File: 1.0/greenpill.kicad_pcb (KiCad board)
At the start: 4 copper layers, 17.4 x 53.1 mm, 33 parts, among them J1 Conn_01x20_Male, J2 Conn_01x20_Male, J3 Conn_01x04_Male, J5 USB_C_Receptacle_USB2.0, SW1 SW_Push, SW2 SW_Push, U1 ATSAMD51J20A-M, U2 MIC5504-3.3YM5, U3 S25FL064, Y1 Crystal_GND23

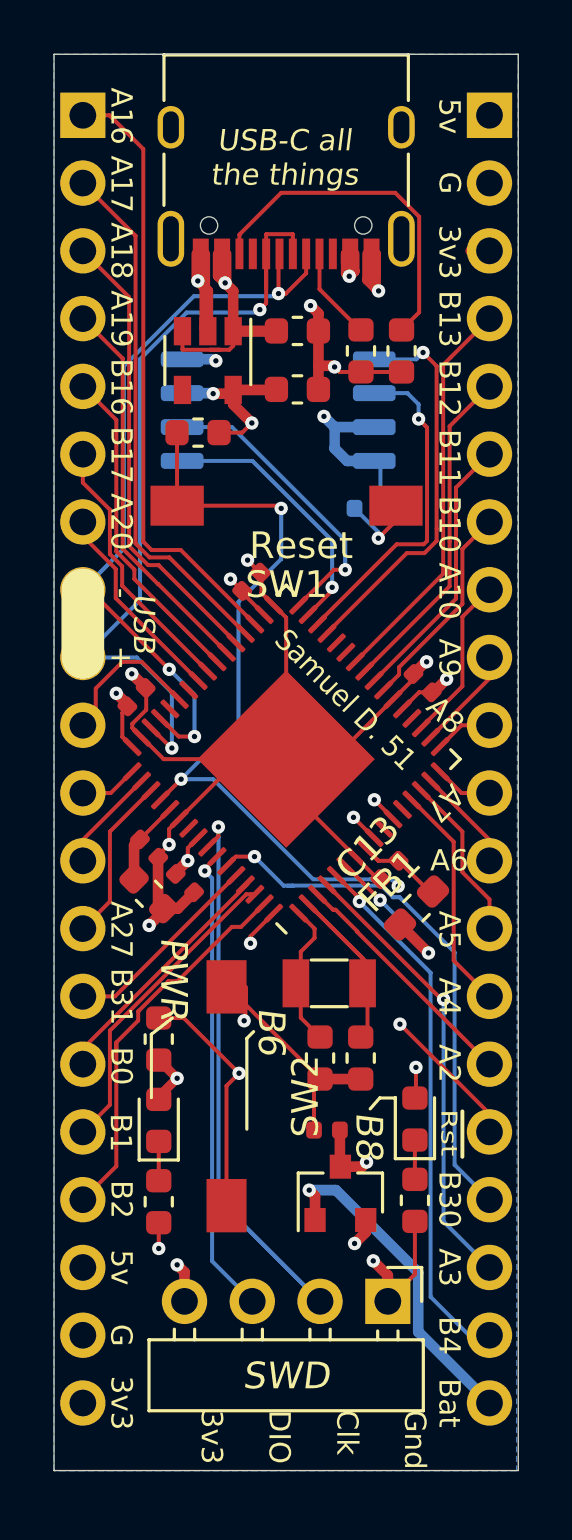
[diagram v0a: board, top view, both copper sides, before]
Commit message: change pinout to hopefully have full timer coverage
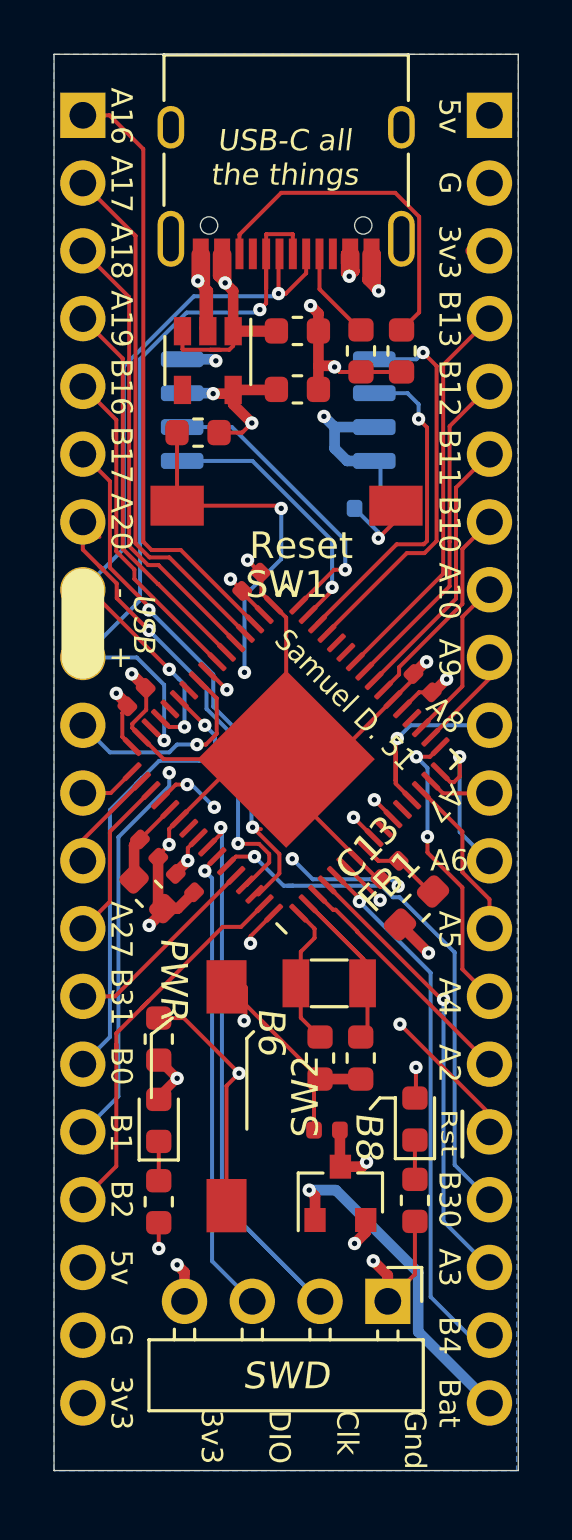
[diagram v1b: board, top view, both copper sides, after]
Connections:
- J1 pad 10: /pa22 -> /pa20
- J1 pad 15: /pb00 -> /pa22
- J1 pad 16: /pb01 -> /pb17
- J1 pad 6: /pb17 -> /pb01
- J1 pad 7: /pa20 -> /pb00
- J2 pad 10: /pa08 -> /pa04
- J2 pad 11: /pa07 -> /pa06
- J2 pad 12: /pa06 -> /pa07
- J2 pad 14: /pa04 -> /pa08
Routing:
- net /pa22: track 5.71 -> 18.3 mm, vias 0 -> 1
- net /pb17: track 10.1 -> 20.4 mm, vias 0 -> 2
- net /pa08: track 2.18 -> 11.2 mm, vias 0 -> 2
- net /pb01: track 11.8 -> 20.4 mm, vias 0 -> 2
- net /pb00: track 9.94 -> 18.4 mm, vias 0 -> 2
- net /pa07: track 2.18 -> 6.02 mm, vias 0 -> 1
- net /pb05: track 3.72 -> 1.83 mm
- net /pa06: track 3.90 -> 2.39 mm
- net /pa04: track 8.57 -> 7.30 mm, vias 0 -> 1
- net /!reset: track 42.3 -> 43.5 mm, vias 4 -> 7
- net /pa24: track 28.5 -> 27.4 mm
- net /pb06: track 24.4 -> 23.5 mm
- net /pa20: track 7.74 -> 8.03 mm, vias 0 -> 1

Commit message: Moved User LED from PB08 to PB09
 - Updated schematic
 - Rerouted trace
 - Updated silkscreen
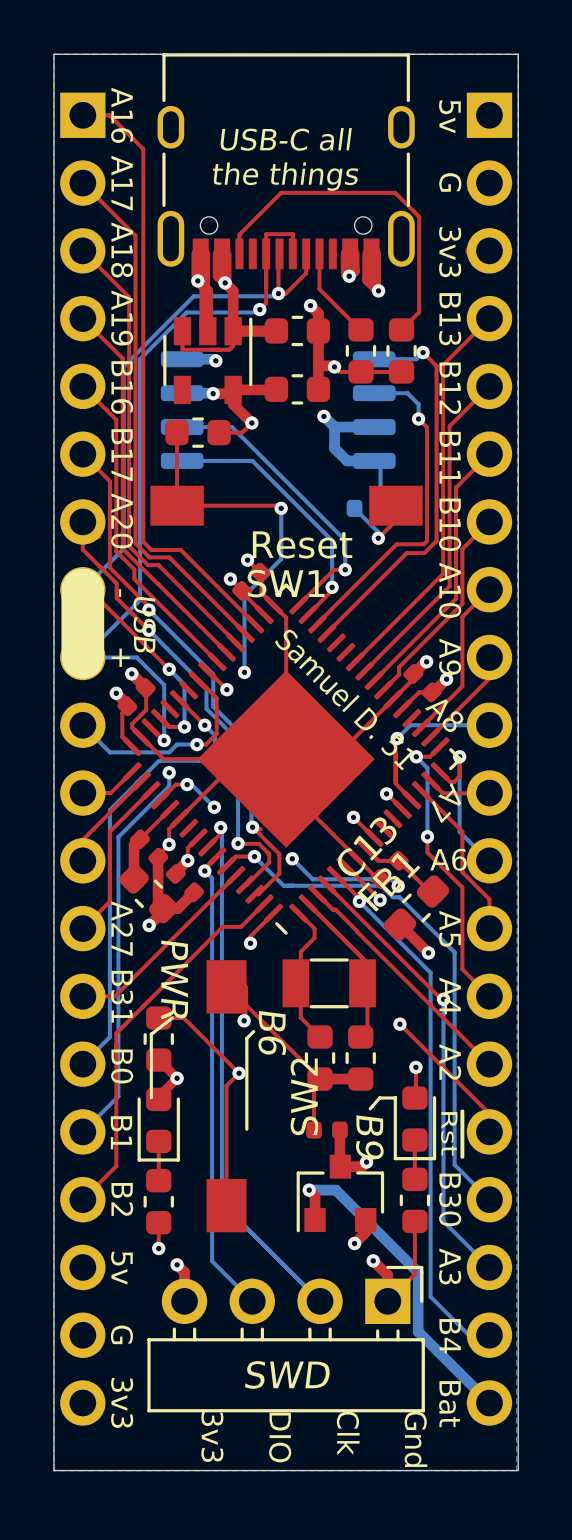
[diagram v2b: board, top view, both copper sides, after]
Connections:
- D2 pad 2: /pb08 -> /pb09
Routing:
- net /pb08: track 13.0 -> 0.01 mm, vias 2 -> 0
- net /pb09: track 0.00 -> 12.8 mm, vias 0 -> 2
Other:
- board text added: "B9"
- board text removed: "B8"

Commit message: Fix silkscreen for new pinout, add PTS636 3D model.
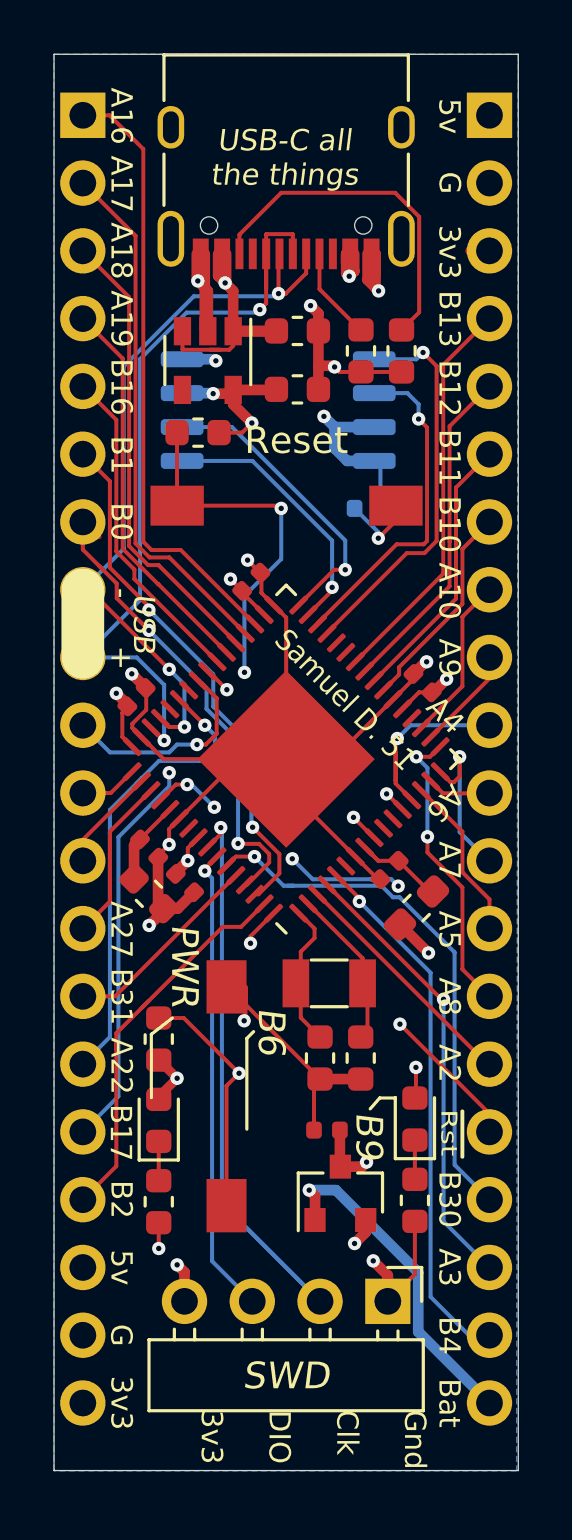
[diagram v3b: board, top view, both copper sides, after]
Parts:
- C13: footprint Resistor_SMD:R_0402_1005Metric -> Capacitor_SMD:C_0402_1005Metric
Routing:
- net /pa01: track 9.85 -> 6.70 mm
- net /pb05: track 1.83 -> 0.01 mm, vias 1 -> 0

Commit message: move silkscreen around on the bottom, add gear logo, adjust copper text
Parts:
- added LOGO1: Logo_Open_Hardware_Small, greenpill:OSHW-Symbol_4x4.5mm_SilkScreen, B.Cu at (136.8, 92.7)

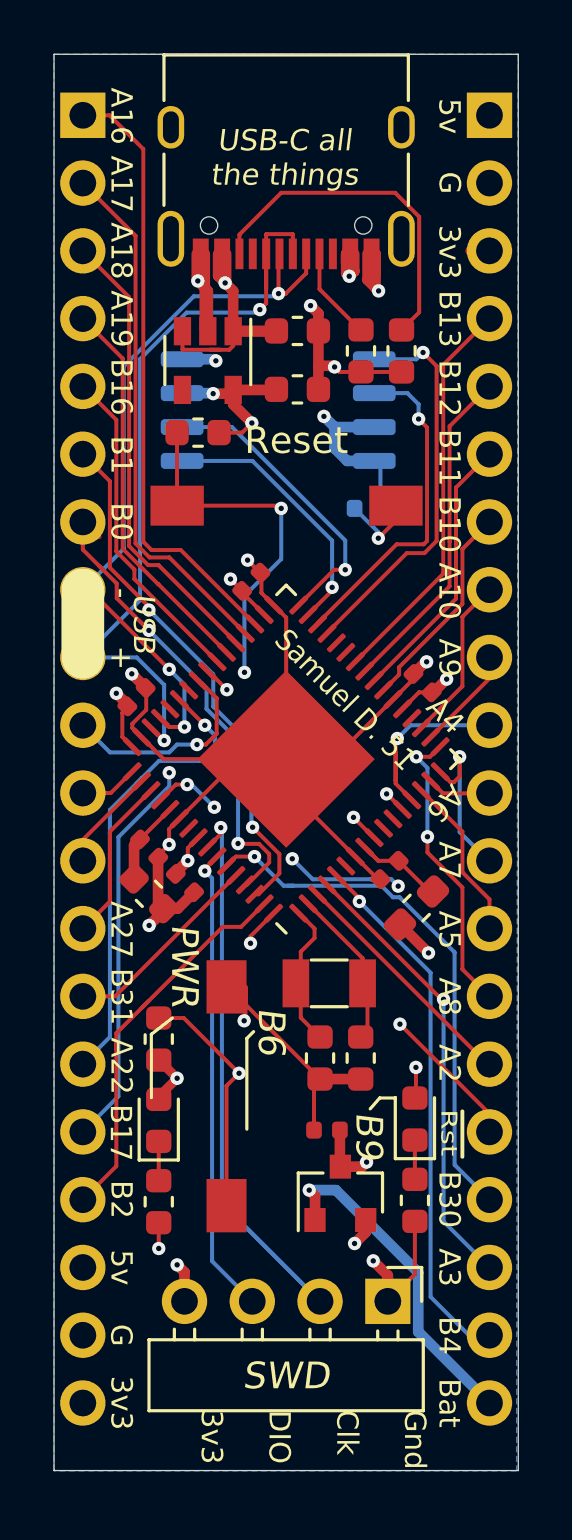
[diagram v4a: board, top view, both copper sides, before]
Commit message: shift around basically all the silkscreen on the back
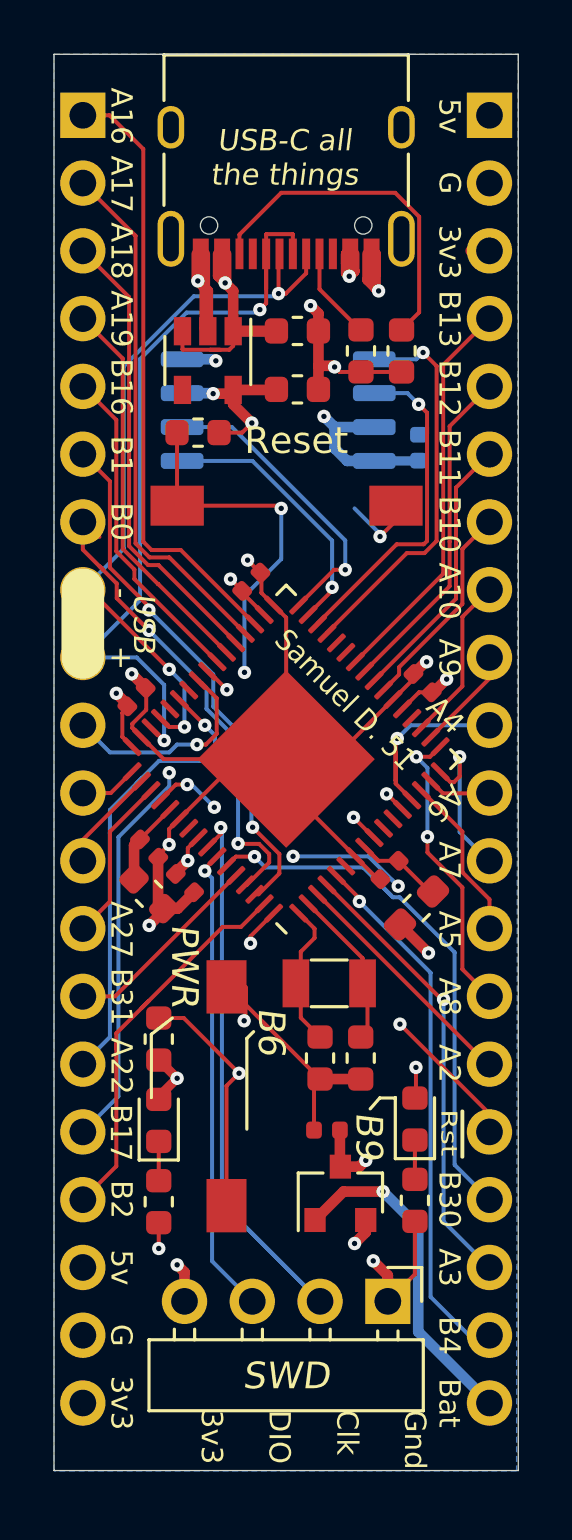
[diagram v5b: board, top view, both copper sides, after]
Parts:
- moved C10 2.97 mm to (140.6, 86.6), turned to 90 degrees
- moved LOGO1 2.44 mm to (137.0, 95.1)
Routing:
- net /!reset: track 43.5 -> 42.8 mm
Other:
- board text added: "batch/board"

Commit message: Moved board/batch number boxes on B.SilkS
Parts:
- removed LOGO1: Logo_Open_Hardware_Small, greenpill:OSHW-Symbol_4x4.5mm_SilkScreen
- added REF**: OSHW-Symbol_6.7x6mm_SilkScreen, Symbol:OSHW-Symbol_6.7x6mm_SilkScreen, B.Cu at (135.8, 93.5)

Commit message: Added r1.0 text
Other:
- board text added: "r1.0"
